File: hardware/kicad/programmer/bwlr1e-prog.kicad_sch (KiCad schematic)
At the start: 46 parts, among them J1 DEBUG, J2 USB_C_Receptacle_USB2.0, J3 RESET, J4 BOOT, Q1 AO3407A, SW1 SW_DIP_x04, SW4 BOOT, SW5 RESET, U1 USBLC6-2P6, U6 CH340E, U7 MCP73831T-2ACI/OT, U8 XC6220B331MR-G

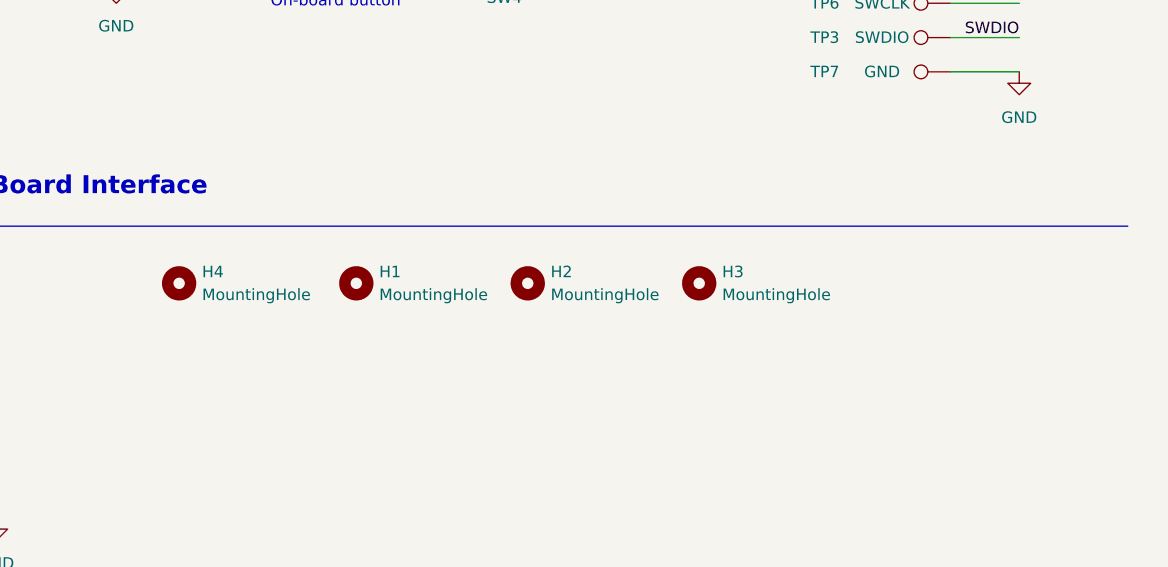
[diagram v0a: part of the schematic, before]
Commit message: fix filter cap footprint
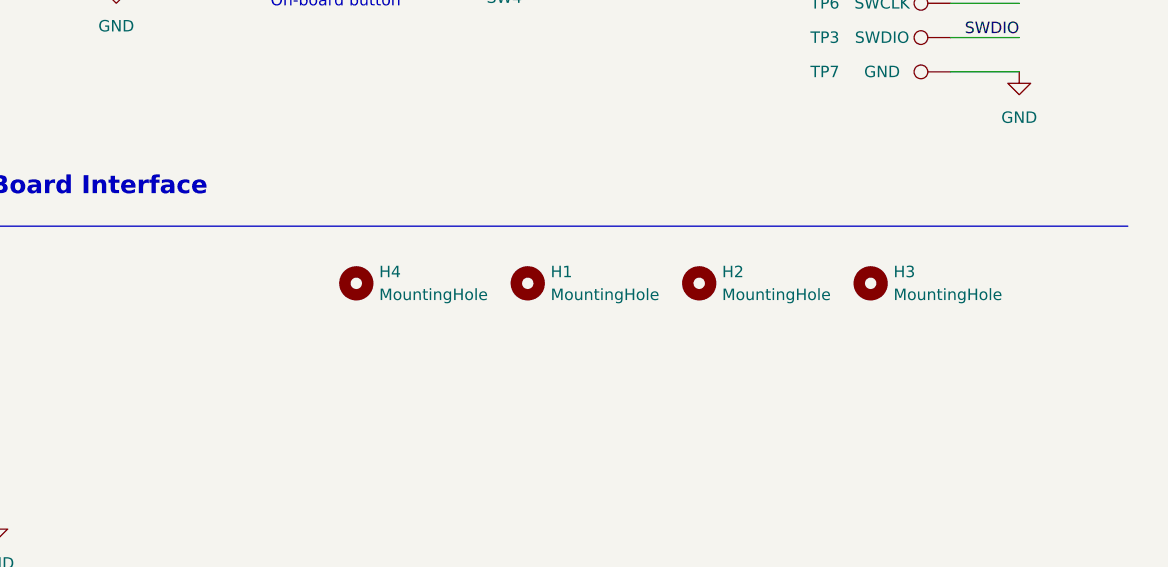
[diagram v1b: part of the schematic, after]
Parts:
- C2, C4: footprint Capacitor_Tantalum_SMD:CP_EIA-3528-15_AVX-H_Pad1.50x2.35mm_HandSolder -> Capacitor_Tantalum_SMD:CP_EIA-3528-15_AVX-H
- TP1: Distributor Link https://www.digikey.com/en/products/detail/preci-dip/90055-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 -> (none)
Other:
- moved on the sheet: H1, H2, H3, H4
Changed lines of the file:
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@@
     )
   )
-  (symbol (lib_id "Mechanical:MountingHole") (at 237.49 159.385 0) (unit 1)
-    (in_bom yes) (on_board yes) (dnp no) (fields_autoplaced)
-    (property "Reference" "H3" (at 240.03 158.115 0)
-      (effects (font (size 1.27 1.27)) (justify left))
-    )
-    (property "Value" "MountingHole" (at 240.03 160.655 0)
-      (effects (font (size 1.27 1.27)) (justify left))
-    )
-    (property "Footprint" "MountingHole:MountingHole_2.2mm_M2" (at 237.49 159.385 0)
-      (effects (font (size 1.27 1.27)) hide)
-    )
-    (property "Datasheet" "~" (at 237.49 159.385 0)
+  (symbol (lib_id "Mechanical:MountingHole") (at 256.54 159.385 0) (unit 1)
+    (in_bom yes) (on_board yes) (dnp no) (fields_autoplaced)
+    (property "Reference" "H3" (at 259.08 158.115 0)
+      (effects (font (size 1.27 1.27)) (justify left))
+    )
+    (property "Value" "MountingHole" (at 259.08 160.655 0)
+      (effects (font (size 1.27 1.27)) (justify left))
+    )
+    (property "Footprint" "MountingHole:MountingHole_2.2mm_M2" (at 256.54 159.385 0)
+      (effects (font (size 1.27 1.27)) hide)
+    )
+    (property "Datasheet" "~" (at 256.54 159.385 0)
       (effects (font (size 1.27 1.27)) hide)
     )
@@
     )
     (property "Part Number" "90055-AS" (at 265.43 109.22 90)
-      (effects (font (size 1.27 1.27)) hide)
-    )
-    (property "Distributor Link" "https://www.digikey.com/en/products/detail/preci-dip/90055-AS/5451878" (at 265.43 109.22 90)
       (effects (font (size 1.27 1.27)) hide)
     )
@@
     )
   )
-  (symbol (lib_id "Mechanical:MountingHole") (at 218.44 159.385 0) (unit 1)
-    (in_bom yes) (on_board yes) (dnp no) (fields_autoplaced)
-    (property "Reference" "H2" (at 220.98 158.115 0)
-      (effects (font (size 1.27 1.27)) (justify left))
-    )
-    (property "Value" "MountingHole" (at 220.98 160.655 0)
-      (effects (font (size 1.27 1.27)) (justify left))
-    )
-    (property "Footprint" "MountingHole:MountingHole_2.2mm_M2" (at 218.44 159.385 0)
-      (effects (font (size 1.27 1.27)) hide)
-    )
-    (property "Datasheet" "~" (at 218.44 159.385 0)
+  (symbol (lib_id "Mechanical:MountingHole") (at 237.49 159.385 0) (unit 1)
+    (in_bom yes) (on_board yes) (dnp no) (fields_autoplaced)
+    (property "Reference" "H2" (at 240.03 158.115 0)
+      (effects (font (size 1.27 1.27)) (justify left))
+    )
+    (property "Value" "MountingHole" (at 240.03 160.655 0)
+      (effects (font (size 1.27 1.27)) (justify left))
+    )
+    (property "Footprint" "MountingHole:MountingHole_2.2mm_M2" (at 237.49 159.385 0)
+      (effects (font (size 1.27 1.27)) hide)
+    )
+    (property "Datasheet" "~" (at 237.49 159.385 0)
       (effects (font (size 1.27 1.27)) hide)
     )
@@
     )
   )
-  (symbol (lib_id "Mechanical:MountingHole") (at 199.39 159.385 0) (unit 1)
-    (in_bom yes) (on_board yes) (dnp no) (fields_autoplaced)
-    (property "Reference" "H1" (at 201.93 158.115 0)
-      (effects (font (size 1.27 1.27)) (justify left))
-    )
-    (property "Value" "MountingHole" (at 201.93 160.655 0)
-      (effects (font (size 1.27 1.27)) (justify left))
-    )
-    (property "Footprint" "MountingHole:MountingHole_2.2mm_M2" (at 199.39 159.385 0)
-      (effects (font (size 1.27 1.27)) hide)
-    )
-    (property "Datasheet" "~" (at 199.39 159.385 0)
+  (symbol (lib_id "Mechanical:MountingHole") (at 218.44 159.385 0) (unit 1)
+    (in_bom yes) (on_board yes) (dnp no) (fields_autoplaced)
+    (property "Reference" "H1" (at 220.98 158.115 0)
+      (effects (font (size 1.27 1.27)) (justify left))
+    )
+    (property "Value" "MountingHole" (at 220.98 160.655 0)
+      (effects (font (size 1.27 1.27)) (justify left))
+    )
+    (property "Footprint" "MountingHole:MountingHole_2.2mm_M2" (at 218.44 159.385 0)
+      (effects (font (size 1.27 1.27)) hide)
+    )
+    (property "Datasheet" "~" (at 218.44 159.385 0)
       (effects (font (size 1.27 1.27)) hide)
     )
@@
     )
   )
-  (symbol (lib_id "Mechanical:MountingHole") (at 179.705 159.385 0) (unit 1)
-    (in_bom yes) (on_board yes) (dnp no) (fields_autoplaced)
-    (property "Reference" "H4" (at 182.245 158.115 0)
-      (effects (font (size 1.27 1.27)) (justify left))
-    )
-    (property "Value" "MountingHole" (at 182.245 160.655 0)
-      (effects (font (size 1.27 1.27)) (justify left))
-    )
-    (property "Footprint" "MountingHole:MountingHole_2.2mm_M2" (at 179.705 159.385 0)
-      (effects (font (size 1.27 1.27)) hide)
-    )
-    (property "Datasheet" "~" (at 179.705 159.385 0)
+  (symbol (lib_id "Mechanical:MountingHole") (at 199.39 159.385 0) (unit 1)
+    (in_bom yes) (on_board yes) (dnp no) (fields_autoplaced)
+    (property "Reference" "H4" (at 201.93 158.115 0)
+      (effects (font (size 1.27 1.27)) (justify left))
+    )
+    (property "Value" "MountingHole" (at 201.93 160.655 0)
+      (effects (font (size 1.27 1.27)) (justify left))
+    )
+    (property "Footprint" "MountingHole:MountingHole_2.2mm_M2" (at 199.39 159.385 0)
+      (effects (font (size 1.27 1.27)) hide)
+    )
+    (property "Datasheet" "~" (at 199.39 159.385 0)
       (effects (font (size 1.27 1.27)) hide)
     )
@@
       (effects (font (size 1.27 1.27)) (justify left))
     )
-    (property "Footprint" "Capacitor_Tantalum_SMD:CP_EIA-3528-15_AVX-H_Pad1.50x2.35mm_HandSolder" (at 53.34 175.895 0)
+    (property "Footprint" "Capacitor_Tantalum_SMD:CP_EIA-3528-15_AVX-H" (at 53.34 175.895 0)
       (effects (font (size 1.27 1.27)) hide)
     )
@@
       (effects (font (size 1.27 1.27)) (justify left))
     )
-    (property "Footprint" "Capacitor_Tantalum_SMD:CP_EIA-3528-15_AVX-H_Pad1.50x2.35mm_HandSolder" (at 41.91 175.895 0)
-      (effects (font (size 1.27 1.27)) hide)
-    )
+    (property "Footprint" "Capacitor_Tantalum_SMD:CP_EIA-3528-15_AVX-H" (at 41.91 175.895 0)
+      (effects (font (size 1.27 1.27)) hide)
+    )

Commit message: update page title
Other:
- title: Teapotlabs BWLR1E -> Teapotlabs BWLR1E Programmer
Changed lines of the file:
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@@
   (paper "A4")
   (title_block
-    (title "Teapotlabs BWLR1E")
-    (date "2023-08-12")
-    (rev "4")
+    (title "Teapotlabs BWLR1E Programmer")
+    (date "2023-09-06")
+    (rev "1")
     (company "Teapot Laboratories")
   )
